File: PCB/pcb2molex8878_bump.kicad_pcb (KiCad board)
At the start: 2 copper layers, 16 x 39 mm, 2 parts

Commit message: fix pocket dims to account for fitment clearance
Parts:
- gave numbers to parts that had none: 1
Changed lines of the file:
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@@
     (descr "Castellated edge contacts to fit Molex 8878 Socket")
     (solder_mask_margin -0.28)
-    (fp_text reference J? (at -0.9906 -0.9906 -90) (layer Dwgs.User) hide
+    (fp_text reference m? (at -0.9906 -0.9906 -90) (layer Dwgs.User) hide
       (effects (font (size 1.2065 1.2065) (thickness 0.127)) (justify left bottom))
     )
@@
       (effects (font (size 1.2065 1.2065) (thickness 0.1016)) (justify left bottom))
     )
+    (fp_line (start 7.2 18.3) (end -7.2 18.3) (layer Dwgs.User) (width 0.01))
+    (fp_line (start 7.2 -18.3) (end 7.2 18.3) (layer Dwgs.User) (width 0.01))
+    (fp_line (start -7.2 -18.3) (end 7.2 -18.3) (layer Dwgs.User) (width 0.01))
+    (fp_line (start -7.2 18.3) (end -7.2 -18.3) (layer Dwgs.User) (width 0.01))
     (fp_arc (start -5.1364 -19.9636) (end -6 -19.9636) (angle -90) (layer Dwgs.User) (width 0.01))
     (fp_text user "actual pcb edge - 0.34\" mill radius" (at -4.05 -19.65) (layer Dwgs.User)
@@
       (effects (font (size 0.2 0.2) (thickness 0.01)))
     )
-    (fp_text user "36.7 x 14.5 x 1.6 pocket" (at -4.4 1.85) (layer Dwgs.User)
+    (fp_text user "36.6 x 14.4 x 1.6 pocket" (at -4.4 1.85) (layer Dwgs.User)
       (effects (font (size 0.2 0.2) (thickness 0.01)))
     )
-    (fp_line (start -7.25 2) (end -6.5 2) (layer Dwgs.User) (width 0.01))
-    (fp_line (start -7.25 2) (end -7 2.25) (layer Dwgs.User) (width 0.01))
-    (fp_line (start -7.25 2) (end -7 1.75) (layer Dwgs.User) (width 0.01))
-    (fp_line (start -7.25 18.35) (end -7.25 -18.35) (layer Dwgs.User) (width 0.01))
-    (fp_line (start 7.25 18.35) (end -7.25 18.35) (layer Dwgs.User) (width 0.01))
-    (fp_line (start 7.25 -18.35) (end 7.25 18.35) (layer Dwgs.User) (width 0.01))
-    (fp_line (start -7.25 -18.35) (end 7.25 -18.35) (layer Dwgs.User) (width 0.01))
+    (fp_line (start -7.2 2) (end -6.45 2) (layer Dwgs.User) (width 0.01))
+    (fp_line (start -7.2 2) (end -6.95 2.25) (layer Dwgs.User) (width 0.01))
+    (fp_line (start -7.2 2) (end -6.95 1.75) (layer Dwgs.User) (width 0.01))
     (fp_line (start 8 19.1) (end 8 -19.1) (layer Eco2.User) (width 0.01))
     (fp_line (start 8 19.1) (end -8 19.1) (layer Eco2.User) (width 0.01))

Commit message: show retainer wedges on pcb drawings. add daughterboard in carrier model.
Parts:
- gave numbers to parts that had none: 2
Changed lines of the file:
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@@
     (descr "Castellated edge contacts to fit Molex 8878 Socket")
     (solder_mask_margin -0.28)
-    (fp_text reference m? (at -0.9906 -0.9906 -90) (layer Dwgs.User) hide
+    (fp_text reference carrier1 (at -0.9906 -0.9906 -90) (layer Dwgs.User) hide
       (effects (font (size 1.2065 1.2065) (thickness 0.127)) (justify left bottom))
     )
@@
       (effects (font (size 1.2065 1.2065) (thickness 0.1016)) (justify left bottom))
     )
+    (fp_text user "10.0 x 1.0 retainer wedges on top surface" (at 0.6 -17.1) (layer Dwgs.User)
+      (effects (font (size 0.2 0.2) (thickness 0.01)))
+    )
+    (fp_line (start -3 -18.1) (end -2.8 -17.9) (layer Dwgs.User) (width 0.01))
+    (fp_line (start -3 -18.1) (end -3.2 -17.9) (layer Dwgs.User) (width 0.01))
+    (fp_line (start -3 -18.1) (end -3 -17) (layer Dwgs.User) (width 0.01))
+    (fp_line (start 5 19.1) (end -5 19.1) (layer Dwgs.User) (width 0.01))
+    (fp_line (start 5 18.1) (end 5 19.1) (layer Dwgs.User) (width 0.01))
+    (fp_line (start -5 18.1) (end 5 18.1) (layer Dwgs.User) (width 0.01))
+    (fp_line (start -5 19.1) (end -5 18.1) (layer Dwgs.User) (width 0.01))
+    (fp_line (start 5 -19.1) (end -5 -19.1) (layer Dwgs.User) (width 0.01))
+    (fp_line (start 5 -18.1) (end 5 -19.1) (layer Dwgs.User) (width 0.01))
+    (fp_line (start -5 -18.1) (end 5 -18.1) (layer Dwgs.User) (width 0.01))
+    (fp_line (start -5 -19.1) (end -5 -18.1) (layer Dwgs.User) (width 0.01))
     (fp_line (start 7.2 18.3) (end -7.2 18.3) (layer Dwgs.User) (width 0.01))
     (fp_line (start 7.2 -18.3) (end 7.2 18.3) (layer Dwgs.User) (width 0.01))
@@
     (descr "Castellated edge contacts to fit Molex 8878 Socket")
     (solder_mask_margin -0.28)
-    (fp_text reference J? (at -0.9906 -0.9906 -90) (layer Dwgs.User) hide
+    (fp_text reference contacts1 (at -0.9906 -0.9906 -90) (layer Dwgs.User) hide
       (effects (font (size 1.2065 1.2065) (thickness 0.127)) (justify left bottom))
     )

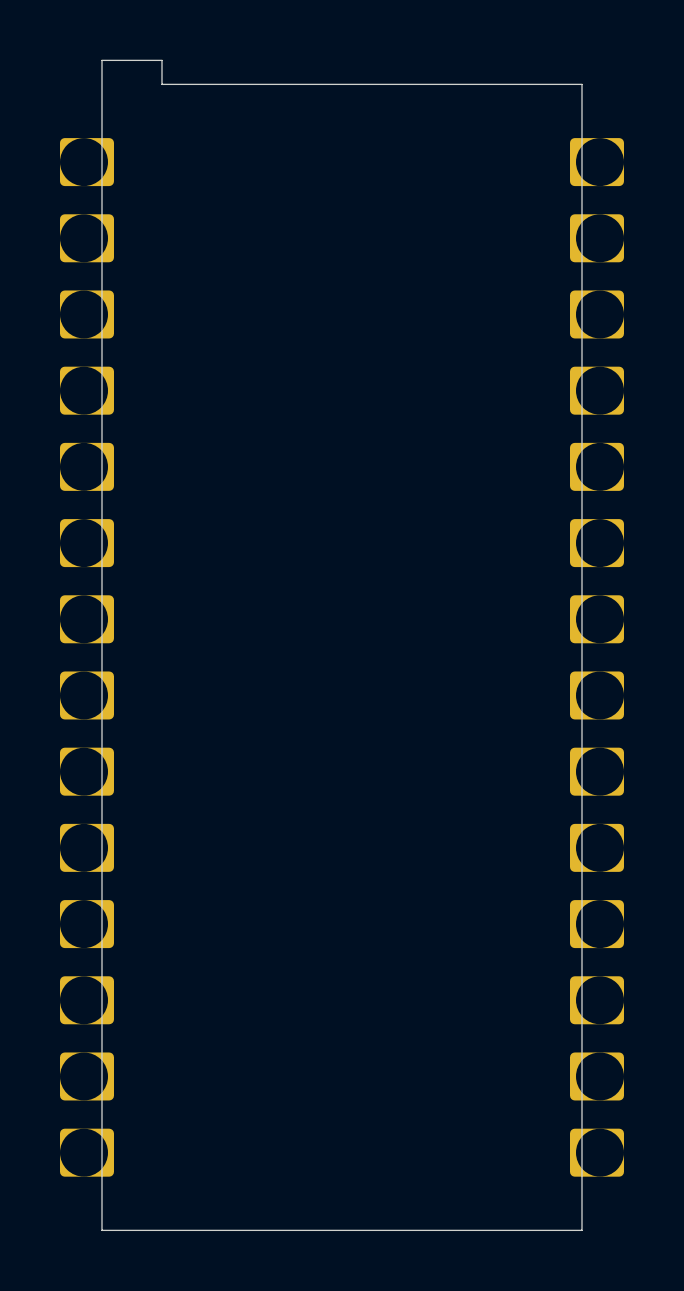
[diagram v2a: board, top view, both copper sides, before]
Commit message: reduce outside X & Y dims by 0.1mm all around
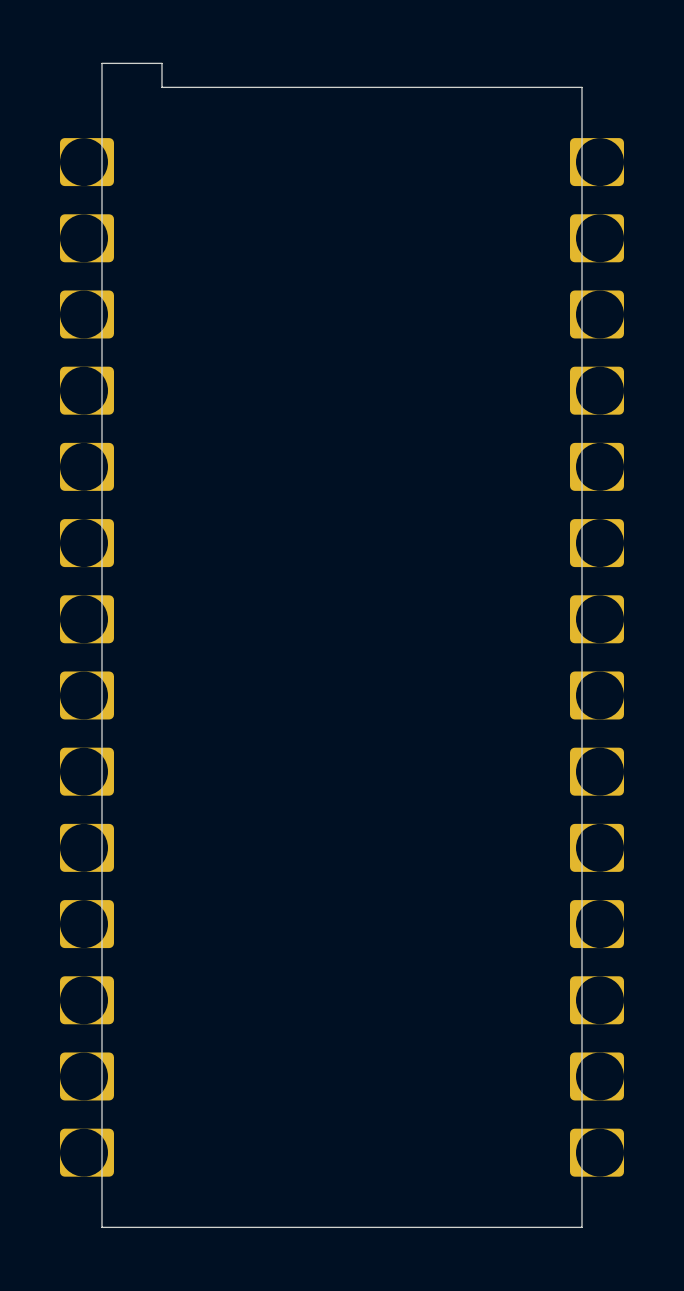
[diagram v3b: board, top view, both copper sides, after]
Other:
- board size 16 x 39 mm -> 16 x 38.8 mm
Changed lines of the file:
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@@
-(kicad_pcb (version 20171130) (host pcbnew 5.1.4-e60b266~84~ubuntu19.04.1)
+(kicad_pcb (version 20171130) (host pcbnew 5.1.5-52549c5~84~ubuntu19.04.1)
   (general
     (thickness 1.6)
@@
       (effects (font (size 1.2065 1.2065) (thickness 0.1016)) (justify left bottom))
     )
-    (fp_text user "10.0 x 1.0 retainer wedges on top surface" (at 0.6 -17.1) (layer Dwgs.User)
-      (effects (font (size 0.2 0.2) (thickness 0.01)))
-    )
-    (fp_line (start -3 -18.1) (end -2.8 -17.9) (layer Dwgs.User) (width 0.01))
-    (fp_line (start -3 -18.1) (end -3.2 -17.9) (layer Dwgs.User) (width 0.01))
-    (fp_line (start -3 -18.1) (end -3 -17) (layer Dwgs.User) (width 0.01))
-    (fp_line (start 5 19.1) (end -5 19.1) (layer Dwgs.User) (width 0.01))
-    (fp_line (start 5 18.1) (end 5 19.1) (layer Dwgs.User) (width 0.01))
-    (fp_line (start -5 18.1) (end 5 18.1) (layer Dwgs.User) (width 0.01))
-    (fp_line (start -5 19.1) (end -5 18.1) (layer Dwgs.User) (width 0.01))
-    (fp_line (start 5 -19.1) (end -5 -19.1) (layer Dwgs.User) (width 0.01))
-    (fp_line (start 5 -18.1) (end 5 -19.1) (layer Dwgs.User) (width 0.01))
-    (fp_line (start -5 -18.1) (end 5 -18.1) (layer Dwgs.User) (width 0.01))
-    (fp_line (start -5 -19.1) (end -5 -18.1) (layer Dwgs.User) (width 0.01))
+    (fp_line (start -4.1 -17.31) (end -3.22 -17.31) (layer Dwgs.User) (width 0.01))
+    (fp_line (start -4.1 -18) (end -4.1 -17.31) (layer Dwgs.User) (width 0.01))
+    (fp_line (start -6.08 -16.51) (end -5.35 -16.51) (layer Dwgs.User) (width 0.01))
+    (fp_line (start -6.08 -18.3) (end -6.08 -16.51) (layer Dwgs.User) (width 0.01))
+    (fp_line (start -6.08 -18.3) (end -6.28 -18.1) (layer Dwgs.User) (width 0.01))
+    (fp_line (start -6.08 -18.3) (end -5.88 -18.1) (layer Dwgs.User) (width 0.01))
+    (fp_text user "10.0 x 1.0 retainer wedges on top surface" (at 0.11 -17.31) (layer Dwgs.User)
+      (effects (font (size 0.2 0.2) (thickness 0.01)))
+    )
+    (fp_line (start -4.1 -18) (end -3.9 -17.8) (layer Dwgs.User) (width 0.01))
+    (fp_line (start -4.1 -18) (end -4.3 -17.8) (layer Dwgs.User) (width 0.01))
+    (fp_line (start 5 19) (end -5 19) (layer Dwgs.User) (width 0.01))
+    (fp_line (start 5 18) (end 5 19) (layer Dwgs.User) (width 0.01))
+    (fp_line (start -5 18) (end 5 18) (layer Dwgs.User) (width 0.01))
+    (fp_line (start -5 19) (end -5 18) (layer Dwgs.User) (width 0.01))
+    (fp_line (start 5 -19) (end -5 -19) (layer Dwgs.User) (width 0.01))
+    (fp_line (start 5 -18) (end 5 -19) (layer Dwgs.User) (width 0.01))
+    (fp_line (start -5 -18) (end 5 -18) (layer Dwgs.User) (width 0.01))
+    (fp_line (start -5 -19) (end -5 -18) (layer Dwgs.User) (width 0.01))
     (fp_line (start 7.2 18.3) (end -7.2 18.3) (layer Dwgs.User) (width 0.01))
     (fp_line (start 7.2 -18.3) (end 7.2 18.3) (layer Dwgs.User) (width 0.01))
     (fp_line (start -7.2 -18.3) (end 7.2 -18.3) (layer Dwgs.User) (width 0.01))
     (fp_line (start -7.2 18.3) (end -7.2 -18.3) (layer Dwgs.User) (width 0.01))
-    (fp_arc (start -5.1364 -19.9636) (end -6 -19.9636) (angle -90) (layer Dwgs.User) (width 0.01))
+    (fp_arc (start -5.1364 -19.8636) (end -6 -19.8636) (angle -90) (layer Dwgs.User) (width 0.01))
     (fp_text user "actual pcb edge - 0.34\" mill radius" (at -4.05 -19.65) (layer Dwgs.User)
       (effects (font (size 0.1 0.1) (thickness 0.01)))
@@
     (fp_line (start -6.3 -19.3) (end -6 -19.3) (layer Dwgs.User) (width 0.01))
     (fp_line (start -6 -19.3) (end -6.3 -19.3) (layer Dwgs.User) (width 0.01))
-    (fp_line (start -6 -19.1) (end 8 -19.1) (layer Eco2.User) (width 0.01))
-    (fp_line (start -8 -19.9) (end -8 19.1) (layer Eco2.User) (width 0.01))
-    (fp_line (start -6 -19.9) (end -6 -19.1) (layer Eco2.User) (width 0.01))
-    (fp_line (start -8 -19.9) (end -6 -19.9) (layer Eco2.User) (width 0.01))
-    (fp_text user "backside components" (at -4.4 2.15) (layer Dwgs.User)
-      (effects (font (size 0.2 0.2) (thickness 0.01)))
-    )
-    (fp_text user "36.6 x 14.4 x 1.6 pocket" (at -4.4 1.85) (layer Dwgs.User)
-      (effects (font (size 0.2 0.2) (thickness 0.01)))
-    )
-    (fp_line (start -7.2 2) (end -6.45 2) (layer Dwgs.User) (width 0.01))
-    (fp_line (start -7.2 2) (end -6.95 2.25) (layer Dwgs.User) (width 0.01))
-    (fp_line (start -7.2 2) (end -6.95 1.75) (layer Dwgs.User) (width 0.01))
-    (fp_line (start 8 19.1) (end 8 -19.1) (layer Eco2.User) (width 0.01))
-    (fp_line (start 8 19.1) (end -8 19.1) (layer Eco2.User) (width 0.01))
-    (fp_line (start -8 -19.1) (end 8 19.1) (layer Dwgs.User) (width 0.01))
-    (fp_line (start -8 19.1) (end 8 -19.1) (layer Dwgs.User) (width 0.01))
+    (fp_line (start -6 -19) (end 8 -19) (layer Eco2.User) (width 0.01))
+    (fp_line (start -8 -19.8) (end -8 19) (layer Eco2.User) (width 0.01))
+    (fp_line (start -6 -19.8) (end -6 -19) (layer Eco2.User) (width 0.01))
+    (fp_line (start -8 -19.8) (end -6 -19.8) (layer Eco2.User) (width 0.01))
+    (fp_text user "36.6 x 14.4 x 1.6 - backside pocket" (at -2.42 -16.5) (layer Dwgs.User)
+      (effects (font (size 0.2 0.2) (thickness 0.01)))
+    )
+    (fp_line (start 8 19) (end 8 -19) (layer Eco2.User) (width 0.01))
+    (fp_line (start 8 19) (end -8 19) (layer Eco2.User) (width 0.01))
     (fp_text user "Eco2.User is Edge.Cuts for use with \"pcb2molex8878_bump\" carrier." (at -0.05 13.65) (layer Eco2.User)
       (effects (font (size 0.2 0.2) (thickness 0.01)))
@@
       (solder_mask_margin -0.19))
   )
-  (gr_line (start 141.2184 80.087) (end 155.2184 80.087) (layer Edge.Cuts) (width 0.0254))
-  (gr_line (start 141.2184 79.287) (end 141.2184 80.087) (layer Edge.Cuts) (width 0.0254))
-  (gr_line (start 139.2184 79.287) (end 141.2184 79.287) (layer Edge.Cuts) (width 0.0254))
-  (gr_line (start 139.2184 118.287) (end 139.2184 79.287) (layer Edge.Cuts) (width 0.0254))
-  (gr_line (start 155.2184 118.287) (end 155.2184 80.087) (layer Edge.Cuts) (width 0.0254))
-  (gr_line (start 139.2184 118.287) (end 155.2184 118.287) (layer Edge.Cuts) (width 0.0254))
+  (gr_line (start 139.2184 79.387) (end 139.2184 118.187) (layer Edge.Cuts) (width 0.0254))
+  (gr_line (start 155.2184 118.187) (end 155.2184 80.187) (layer Edge.Cuts) (width 0.0254))
+  (gr_line (start 141.2184 80.187) (end 155.2184 80.187) (layer Edge.Cuts) (width 0.0254))
+  (gr_line (start 141.2184 79.387) (end 141.2184 80.187) (layer Edge.Cuts) (width 0.0254))
+  (gr_line (start 139.2184 79.387) (end 141.2184 79.387) (layer Edge.Cuts) (width 0.0254))
+  (gr_line (start 139.2184 118.187) (end 155.2184 118.187) (layer Edge.Cuts) (width 0.0254))
 )
